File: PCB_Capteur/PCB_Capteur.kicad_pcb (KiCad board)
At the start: 2 copper layers, 66 x 61 mm, 15 parts, among them J1 Conn_01x08_Socket, J2 Conn_ESP32_Custom, J3 Conn_01x02_Socket, U1 DM-OLED096-636

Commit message: PCB Improvements
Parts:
- moved R6 65.7 mm to (156.5, 83.9), turned to -90 degrees
- moved R1 59.3 mm to (153.0, 84.0), turned to 180 degrees
- moved C2 53.5 mm to (96.0, 59.5), turned to -90 degrees
- moved LTC1050 49.2 mm to (138.0, 93.0), turned to 0 degrees
- moved C1 41.5 mm to (134.5, 84.5), turned to 0 degrees
- moved J3 35.9 mm to (95.0, 102.8), turned to 180 degrees
- moved R5 23.2 mm to (152.6, 104.5)
- moved R7 21.4 mm to (129.5, 94.6), turned to 90 degrees
- moved J1 13.6 mm to (103.2, 103.5)
- moved C4 12.5 mm to (146.5, 93.5), turned to 90 degrees
- moved R4 12.0 mm to (142.4, 97.5), turned to 0 degrees
- moved R2 8.31 mm to (152.6, 101.0)
- moved J2 5.70 mm to (113.5, 74.5)
- moved GazSensor 5.39 mm to (133.0, 105.0), turned to 90 degrees
- moved U1 1.58 mm to (141.0, 68.5), turned to 180 degrees
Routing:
- net Net-(LTC1050--IN): track 112.6 -> 37.8 mm, vias 2 -> 0
- net Net-(LTC1050-OUT): track 97.6 -> 38.9 mm, vias 2 -> 0
- net Net-(LTC1050-+IN): track 86.2 -> 44.4 mm, vias 3 -> 1
- net +5V: track 102.9 -> 61.3 mm
- net 15V: track 5.25 -> 44.8 mm
- net ADC: track 69.1 -> 101.1 mm
- net GND: track 164.6 -> 144.2 mm, vias 0 -> 1
- net TX: track 51.4 -> 34.5 mm, vias 1 -> 0
- net RST: track 42.9 -> 26.3 mm, vias 1 -> 0
- net TempSensor: track 75.0 -> 63.1 mm, vias 0 -> 1
- net RX: track 50.7 -> 42.0 mm
- net OLED_SDA: track 25.8 -> 18.2 mm
- net OLED_SCL: track 20.1 -> 26.9 mm
- net +3.3V: track 41.4 -> 34.9 mm
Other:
- board size 66 x 61 mm -> 67.5 x 54 mm

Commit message: PCB Optimizations
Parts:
- C1, C4, GazSensor, LTC1050, R1, R2, R4, R5, R6, R7: moved to B.Cu
- moved R6 53.6 mm to (102.9, 83.0), turned to 0 degrees
- moved GazSensor 43.5 mm to (118.6, 63.9)
- moved C4 43.4 mm to (108.0, 73.5), turned to 180 degrees
- moved R1 41.7 mm to (111.5, 80.1), turned to 90 degrees
- moved R7 41.0 mm to (113.2, 57.0), turned to 180 degrees
- moved R2 39.9 mm to (118.6, 80.1), turned to 90 degrees
- moved LTC1050 39.9 mm to (110.6, 64.0), turned to -90 degrees
- moved R5 39.2 mm to (122.0, 80.0), turned to 90 degrees
- moved R4 38.8 mm to (115.1, 69.9), turned to -90 degrees
- moved C1 38.1 mm to (104.1, 61.5), turned to -90 degrees
- moved C2 0.50 mm to (95.5, 59.5)
- turned U1 to 90 degrees
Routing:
- net ADC: track 101.1 -> 31.3 mm
- net GND: track 144.2 -> 188.4 mm, vias 1 -> 2
- net TempSensor: track 63.1 -> 21.1 mm, vias 1 -> 0
- net +5V: track 61.3 -> 97.2 mm, vias 2 -> 4
- net +3.3V: track 34.9 -> 58.8 mm, vias 0 -> 1
- net OLED_SCL: track 26.9 -> 9.86 mm
- net OLED_SDA: track 18.2 -> 5.27 mm
- net 15V: track 44.8 -> 55.8 mm, vias 0 -> 1
- net Net-(LTC1050-+IN): track 44.4 -> 34.5 mm, vias 1 -> 0
- net RX: track 42.0 -> 33.1 mm, vias 1 -> 0
- net TX: track 34.5 -> 43.2 mm, vias 0 -> 1
- net Net-(LTC1050-OUT): track 38.9 -> 42.9 mm
- net Net-(LTC1050--IN): track 37.8 -> 34.8 mm, vias 0 -> 1
- net GazSensor1: track 8.17 -> 10.4 mm
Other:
- board size 67.5 x 54 mm -> 40 x 54 mm

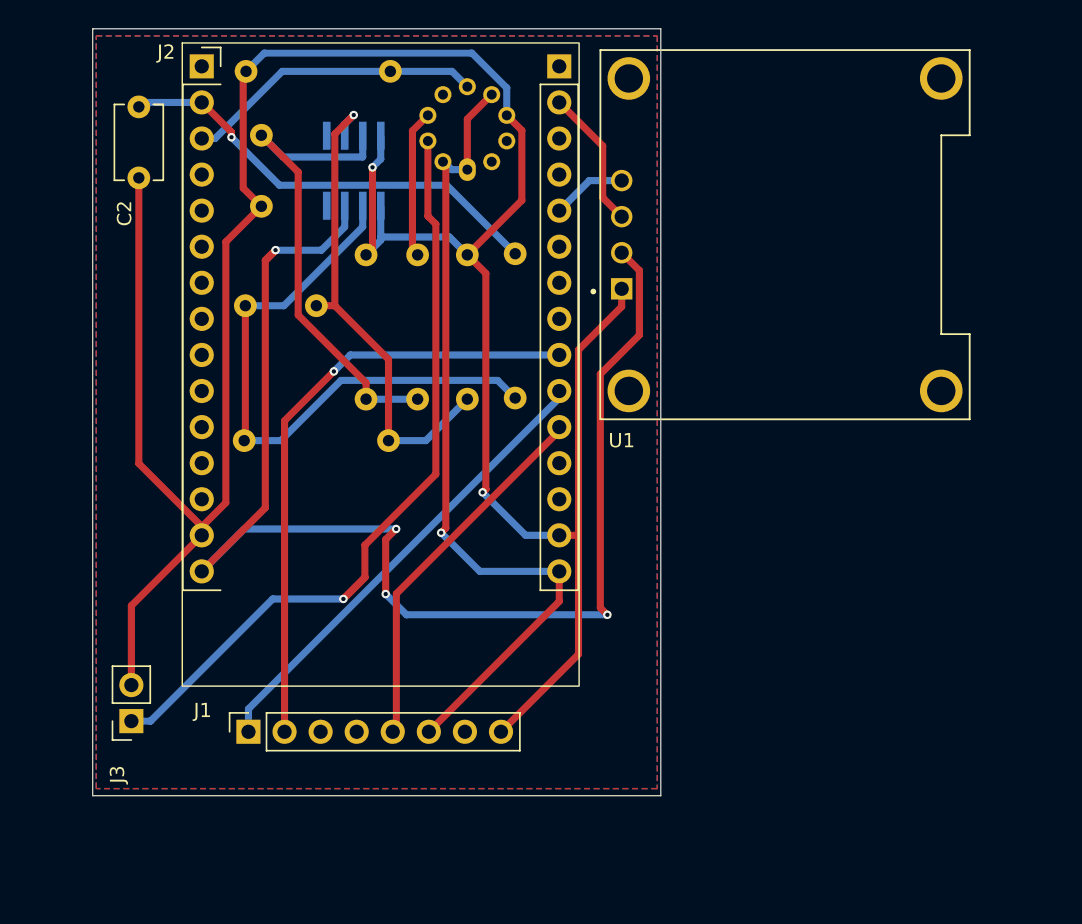
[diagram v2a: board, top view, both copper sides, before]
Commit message: Adding Images for the readme
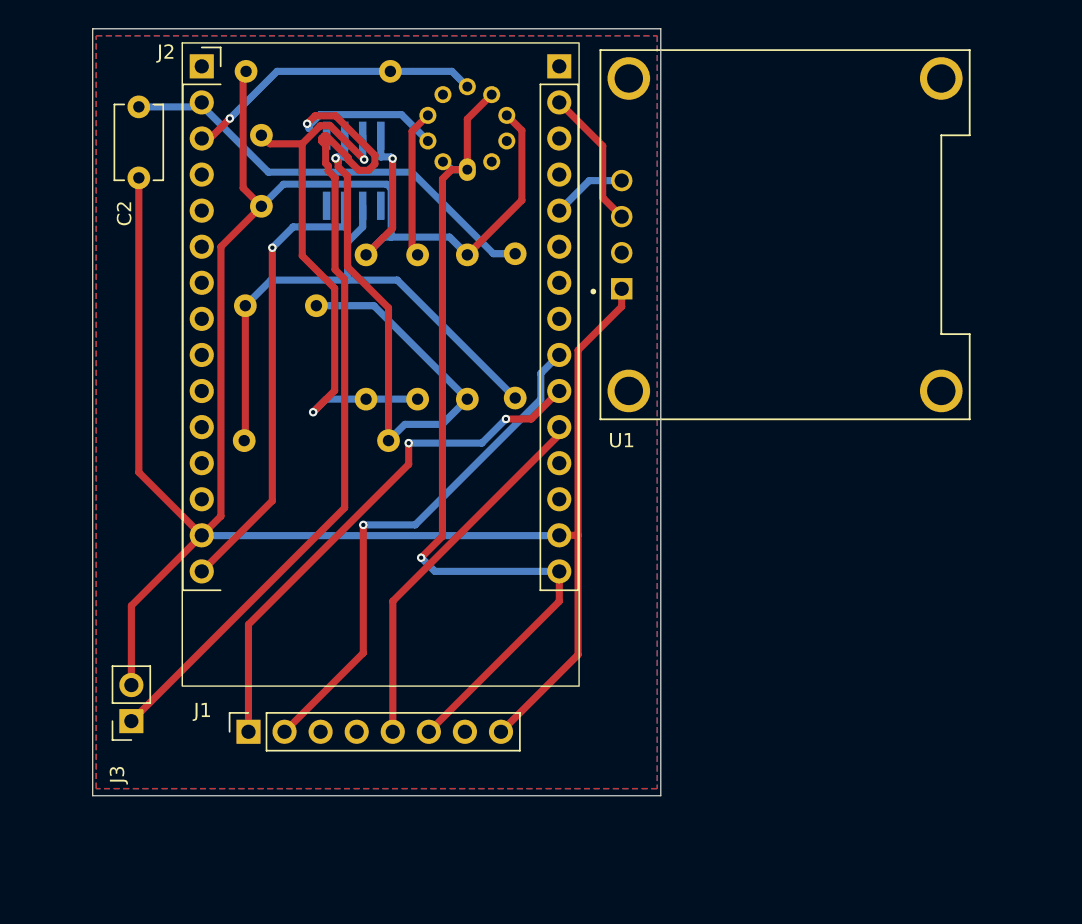
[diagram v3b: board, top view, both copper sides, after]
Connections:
- LTC1050 pad 5: GND -> unconnected-(LTC1050-CLK-Pad5)
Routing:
- net +5V: track 97.2 -> 32.0 mm, vias 4 -> 1
- net 15V: track 55.8 -> 69.9 mm
- net GND: track 188.4 -> 179.1 mm, vias 2 -> 1
- net Net-(LTC1050--IN): track 34.8 -> 43.7 mm
- net TX: track 43.2 -> 36.7 mm
- net Net-(LTC1050-OUT): track 42.9 -> 38.4 mm
- net Net-(LTC1050-+IN): track 34.5 -> 38.9 mm, vias 0 -> 2
- net RX: track 33.1 -> 37.1 mm, vias 0 -> 2
- net +3.3V: track 58.8 -> 62.5 mm
- net ADC: track 31.3 -> 31.2 mm, vias 1 -> 0
- net TempSensor: vias 0 -> 1
